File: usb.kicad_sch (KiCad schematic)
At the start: 11 parts, among them J1 USB_C, U15 TVS_USB, U29 FUSB302B, U30 DPO2036

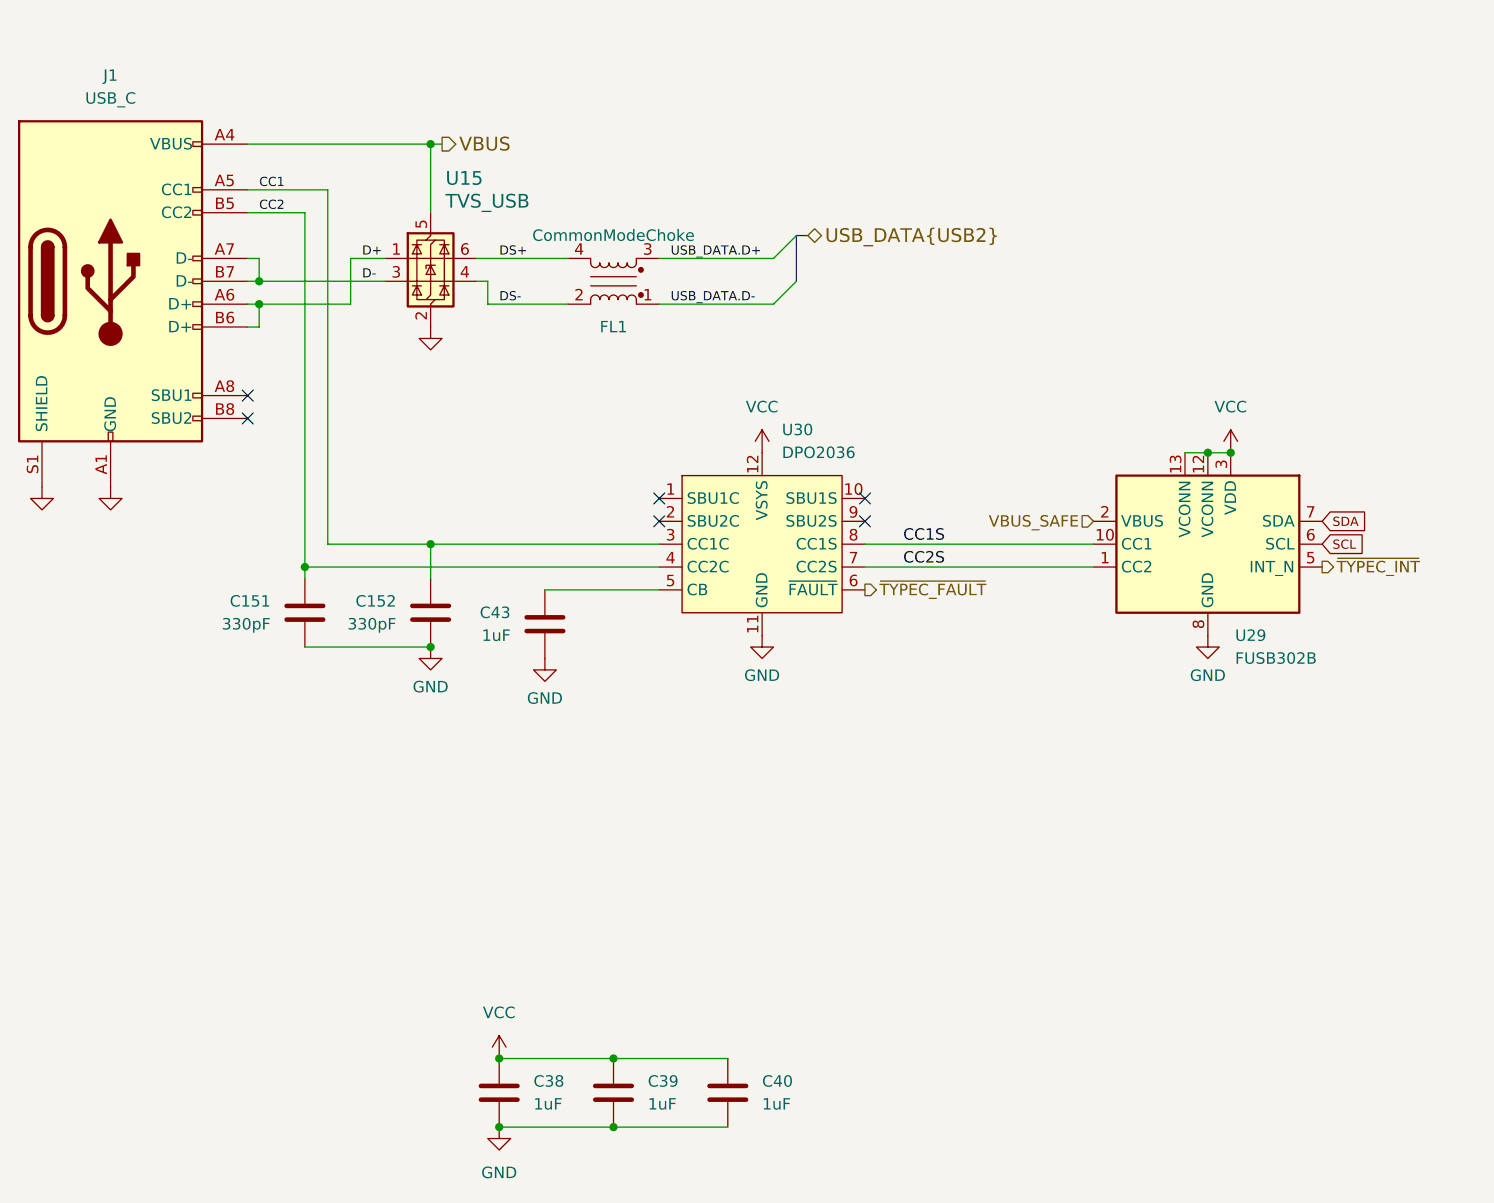
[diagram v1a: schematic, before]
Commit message: Change Type-C controller U29 to HUSB328
- Update USB TVS
- Improve USB differential impedance
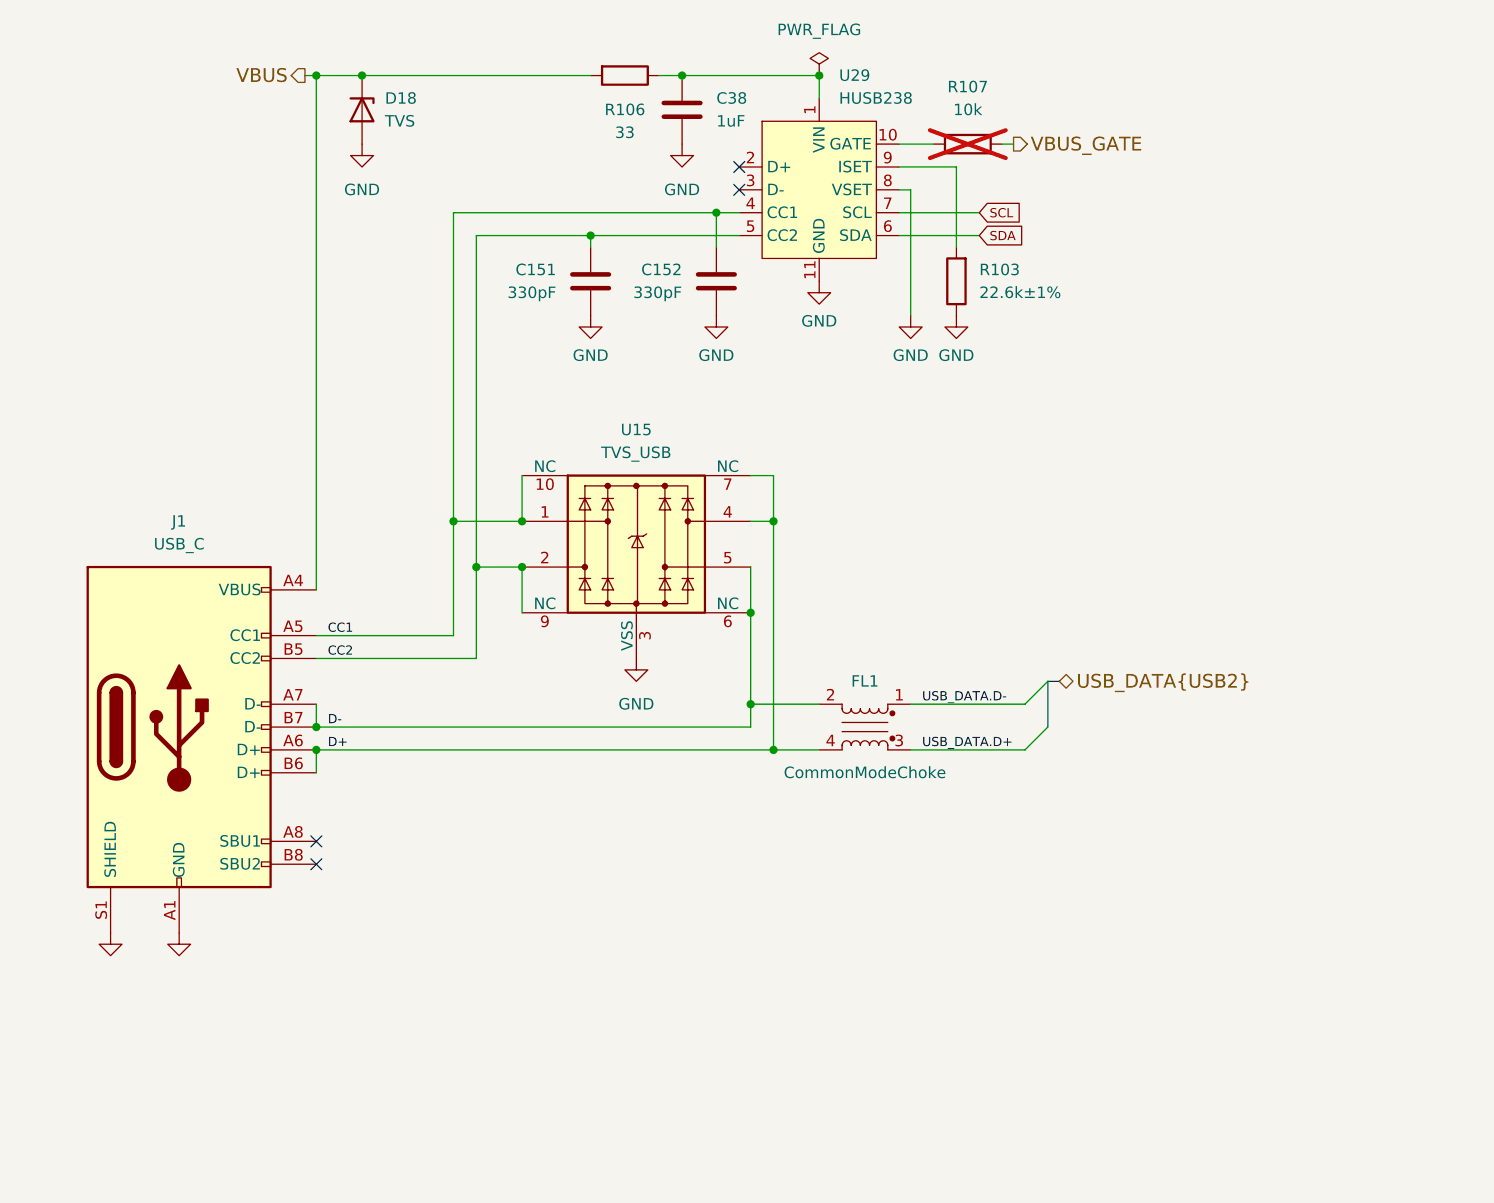
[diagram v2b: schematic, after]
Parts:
- removed C39, C40, C43: 1uF, Capacitor_SMD:C_0402_1005Metric, symbol Device:C
- removed U15: TVS_USB, Package_TO_SOT_SMD:SOT-563, symbol Power_Protection:USBLC6-2P6
- removed U29: FUSB302B, Package_DFN_QFN:WQFN-14-1EP_2.5x2.5mm_P0.5mm_EP1.45x1.45mm, symbol Interface_USB:FUSB302BMPX
- removed U30: DPO2036, praline:Diodes_UQFN2020-12_Type-B, symbol praline:DPO2036
- added D18: TVS, praline:DFN1006-2, symbol Device:D_Zener
- added R103: 22.6k±1%, Resistor_SMD:R_0201_0603Metric, symbol Device:R
- added R106: 33, Resistor_SMD:R_0402_1005Metric, symbol Device:R
- added R107: 10k, Resistor_SMD:R_0402_1005Metric, symbol Device:R
- added U15: TVS_USB, Package_DFN_QFN:Diodes_UDFN-10_1.0x2.5mm_P0.5mm, symbol Power_Protection:D3V3XA4B10LP
- added U29: HUSB238, Package_DFN_QFN:WDFN-10-1EP_3x3mm_P0.5mm_EP1.8x2.5mm, symbol praline:HUSB238
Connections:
- net DS+ is gone; now on net D+: FL1.4
- net DS- is gone; now on net D-: FL1.2
- net CC1: now also U15.1, U15.10 (NC), U29.4 (CC1)
- net CC2: now also U15.2, U15.9 (NC), U29.5 (CC2)
- net D+: now also U15.4, U15.7 (NC)
- net D-: now also U15.5, U15.6 (NC)
- net GND: now also D18.2 (A), R103.1, U15.3 (VSS), U15.8 (VSS), U29.11 (GND), U29.8 (VSET)
- net SCL: now also U29.7 (SCL)
- net SDA: now also U29.6 (SDA)
- net VBUS: now also D18.1 (K), R106.2
- net VCC: no longer names the net of C38.1
- net VCC: now also R106.1, U29.1 (VIN)
- new net: R103.2, U29.9 (ISET)
- new net: R107.1, U29.10 (GATE)
- new net VBUS_GATE: R107.2
- no-connect marks 6 -> 4
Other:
- moved on the sheet: C151, C152, C38, FL1, J1

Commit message: Connect mixer U4 LD and ENBL pins to MCU
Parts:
- C151, C152: Manufacturer Murata -> Murata
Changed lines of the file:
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@@
 			)
 		)
-		(property "Manufacturer" "Murata "
+		(property "Manufacturer" "Murata"
 			(at 135.89 71.12 0)
 			(effects
@@
 			)
 		)
-		(property "Manufacturer" "Murata "
+		(property "Manufacturer" "Murata"
 			(at 149.86 71.12 0)
 			(effects

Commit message: Update TVS
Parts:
- U15: Manufacturer Msksemi -> TECH PUBLIC; Part Number RClamp0524P.TCT-MS -> TPAZ1143-04F
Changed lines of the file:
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@@
 			)
 		)
-		(property "Datasheet" "https://www.msksemi.com/web/userfiles/productfile/C3008054RClamp0524P.TCT-MS.pdf"
+		(property "Datasheet" "https://www.techpublic.com/storage/pdf/20230509/guMCHlfdvJyXLYRZ.pdf"
 			(at 140.97 100.33 0)
 			(effects
@@
 			)
 		)
-		(property "Manufacturer" "Msksemi"
+		(property "Manufacturer" "TECH PUBLIC"
 			(at 140.97 100.33 0)
 			(effects
@@
 			)
 		)
-		(property "Part Number" "RClamp0524P.TCT-MS"
+		(property "Part Number" "TPAZ1143-04F"
 			(at 140.97 100.33 0)
 			(effects

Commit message: Update to KiCad 9
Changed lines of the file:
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@@
 (kicad_sch
-	(version 20231120)
+	(version 20250114)
 	(generator "eeschema")
-	(generator_version "8.0")
+	(generator_version "9.0")
 	(paper "A4")
 	(title_block

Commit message: Update symbols and footprints
- Update U21 symbol and footprint
- Add L10, L11 3D model
- Add T1, T2 3D model
- Update U29 footprint
- Update J10 footprint and part selection, change to TP6
- Update diode footprints and 3D models
- Update SMA connector footprint
- Fix 3D model scale for various footprints
- Change L1 from 0603 back to 0201
- Fix pin header 3D models
- Add component substitutions
- Update RF switch and amplifier footprints
- Remove fiducials
- Update mounting hole symbol and footprint
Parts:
- U29: footprint Package_DFN_QFN:WDFN-10-1EP_3x3mm_P0.5mm_EP1.8x2.5mm -> praline:WDFN-10-1EP_3x3mm_P0.5mm_EP1.8x2.5mm_ThermalVias
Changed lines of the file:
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@@
 			)
 		)
-		(property "Footprint" "Package_DFN_QFN:WDFN-10-1EP_3x3mm_P0.5mm_EP1.8x2.5mm"
+		(property "Footprint" "praline:WDFN-10-1EP_3x3mm_P0.5mm_EP1.8x2.5mm_ThermalVias"
 			(at 161.29 78.74 0)
 			(effects

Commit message: Use consistent footprints for 0402 and 0201 diodes
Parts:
- D18: footprint praline:DFN1006-2 -> praline:TSLP-2-19
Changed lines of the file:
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@@
 			)
 		)
-		(property "Footprint" "praline:DFN1006-2"
+		(property "Footprint" "praline:TSLP-2-19"
 			(at 110.49 52.07 0)
 			(effects

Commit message: Standardize component Value fields
Use Tolerance field instead of expressing tolerance in Value field
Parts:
- C151, C152: value 330pF -> 330 pF
- C38: value 1uF -> 1 uF
- R103: value 22.6k±1% -> 22.6k; Tolerance (none) -> ±1%
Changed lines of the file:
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@@
 		(fields_autoplaced yes)
 		(property "Reference" "R103"
-			(at 179.07 69.8499 0)
+			(at 179.07 68.5799 0)
 			(effects
 				(font
@@
 			)
 		)
-		(property "Value" "22.6k±1%"
-			(at 179.07 72.3899 0)
+		(property "Value" "22.6k"
+			(at 179.07 71.1199 0)
 			(effects
 				(font
@@
 			)
 		)
+		(property "Tolerance" "±1%"
+			(at 179.07 73.6599 0)
+			(effects
+				(font
+					(size 1.27 1.27)
+				)
+				(justify right)
+			)
+		)
 		(pin "1"
 		)
@@
 			)
 		)
-		(property "Value" "330pF"
+		(property "Value" "330 pF"
 			(at 132.08 72.3899 0)
 			(effects
@@
 			)
 		)
-		(property "Value" "1uF"
+		(property "Value" "1 uF"
 			(at 149.86 53.3399 0)
 			(effects
@@
 			)
 		)
-		(property "Value" "330pF"
+		(property "Value" "330 pF"
 			(at 146.05 72.3899 0)
 			(effects
